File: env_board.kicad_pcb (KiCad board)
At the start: 2 copper layers, 22.5 x 29 mm, 30 parts, among them J1 CONN_01X07, J2 BATT_CONN, P1 USB_OTG, Q1 NX7002AKVL, Q2 DMP3099L-13, Q3 DMP3099L-13, U1 RFD77101, U2 ENS210, U3 CCS811, U4 TLV74130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

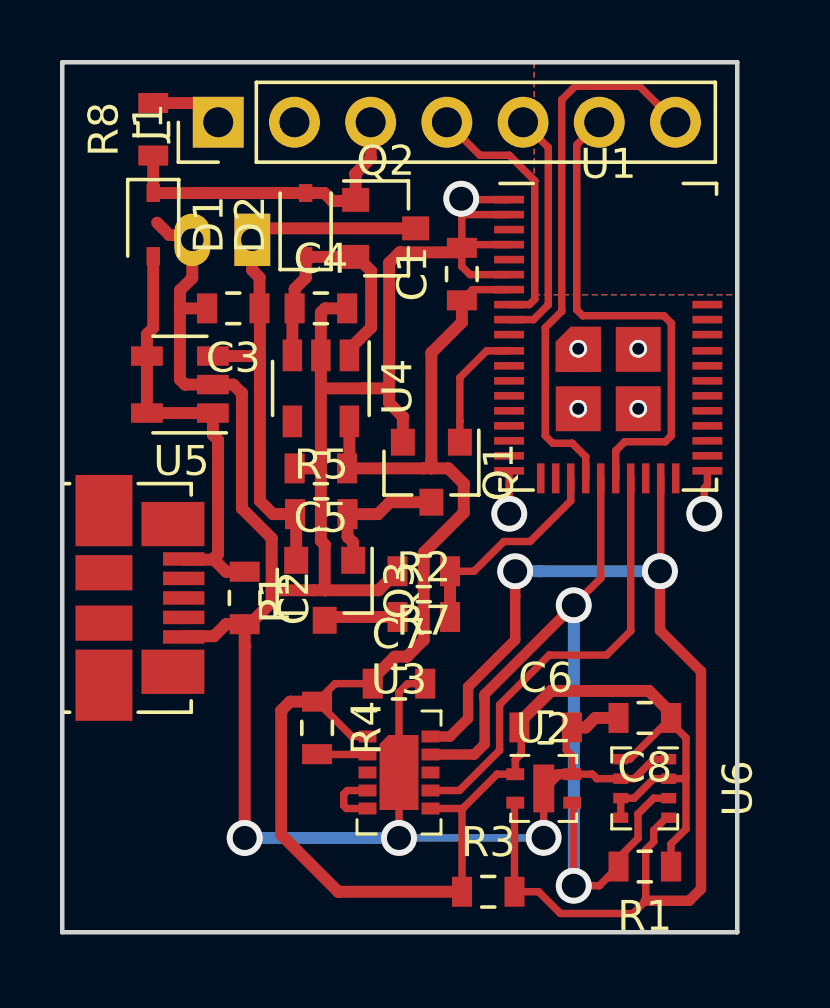
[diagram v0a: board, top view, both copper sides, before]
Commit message: add flash memory
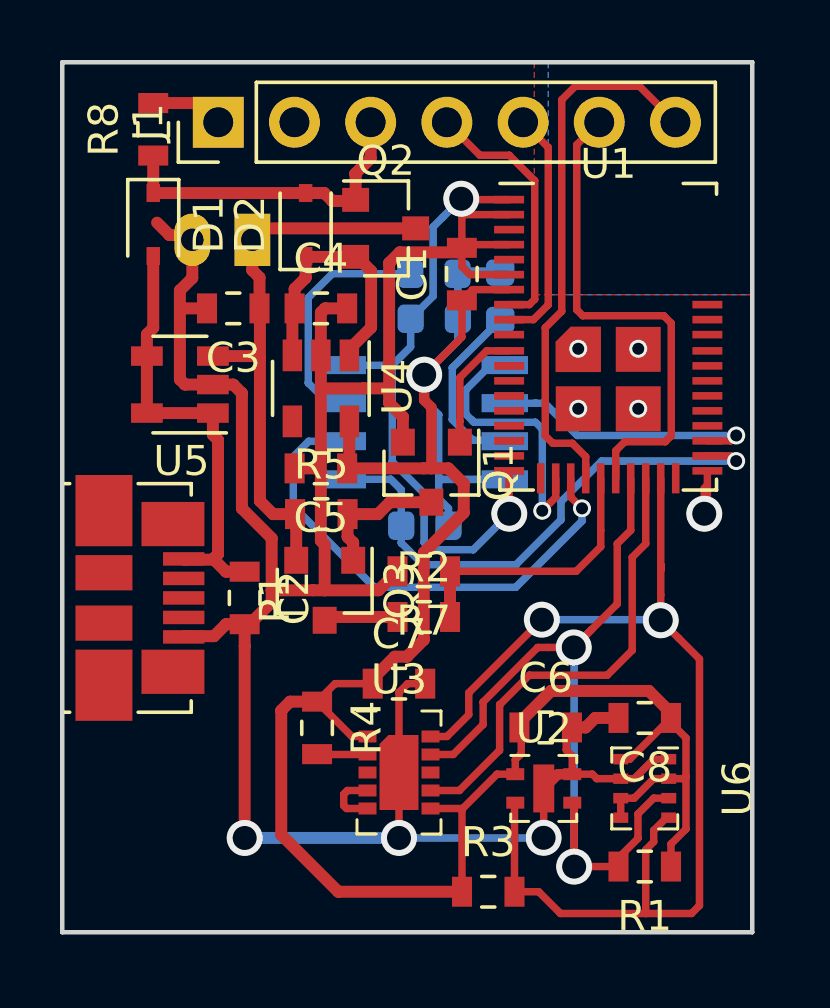
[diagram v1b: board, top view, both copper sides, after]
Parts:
- added C9: 0.1u, Capacitor_SMD:C_0603_1608Metric, B.Cu at (158.7, 105.5)
- added R10: 100k, Resistor_SMD:R_0603_1608Metric, B.Cu at (158.4, 112.5)
- added R6: 100k, Resistor_SMD:R_0603_1608Metric, B.Cu at (160.9, 104.8)
- added R9: 100k, Resistor_SMD:R_0603_1608Metric, B.Cu at (158.7, 104.0)
- added U7: SST26VF016B, Package_SO:SOIC-8_3.9x4.9mm_P1.27mm, B.Cu at (158.3, 109.0)
- moved G*** 18.7 mm to (151.5, 120.8)
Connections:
- U1 pad 21: (no net) -> /FLASH_SI
- U1 pad 22: /BATT_V -> /FLASH_SO
- U1 pad 24: /SDA -> /BATT_V
- U1 pad 26: /CCS_WAKE -> /SDA
- U1 pad 27: (no net) -> /CCS_WAKE
- U1 pad 31: (no net) -> /FLASH_CS
- U1 pad 32: (no net) -> /FLASH_SCK
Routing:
- net GND: track 94.8 -> 113.7 mm
- net /FLASH_CS: track 0.00 -> 18.2 mm, vias 0 -> 1
- net /FLASH_SO: track 0.00 -> 16.7 mm, vias 0 -> 1
- net VDD: track 62.7 -> 76.2 mm, vias 0 -> 1
- net /FLASH_SI: track 0.00 -> 9.30 mm, vias 0 -> 1
- net /FLASH_SCK: track 0.00 -> 9.20 mm, vias 0 -> 1
- net Net-(R9-Pad2): track 0.00 -> 8.00 mm
- net Net-(R6-Pad2): track 0.00 -> 6.04 mm
- net /BATT_V: track 7.44 -> 9.33 mm
- net /SDA: track 29.6 -> 28.2 mm
- net /SCL: track 39.2 -> 37.9 mm
- net /CCS_WAKE: track 14.9 -> 15.5 mm
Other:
- board size 22.5 x 29 mm -> 23 x 29 mm
